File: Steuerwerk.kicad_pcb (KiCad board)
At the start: 2 copper layers, 100 x 160 mm, 115 parts, among them J1 Conn_01x04, J2 Conn_01x02, J3 Conn_01x03, J4 Conn_01x03, J5 Conn_01x02, J6 Conn_01x04, J7 Conn_01x02, J8 Conn_01x04, Q1 Q_PNP_BCE, U1 74LS161, U2 74LS138, U3 74LS138, U4 74240, U5 74LS374, U6 74LS374, U7 74541, U8 74541

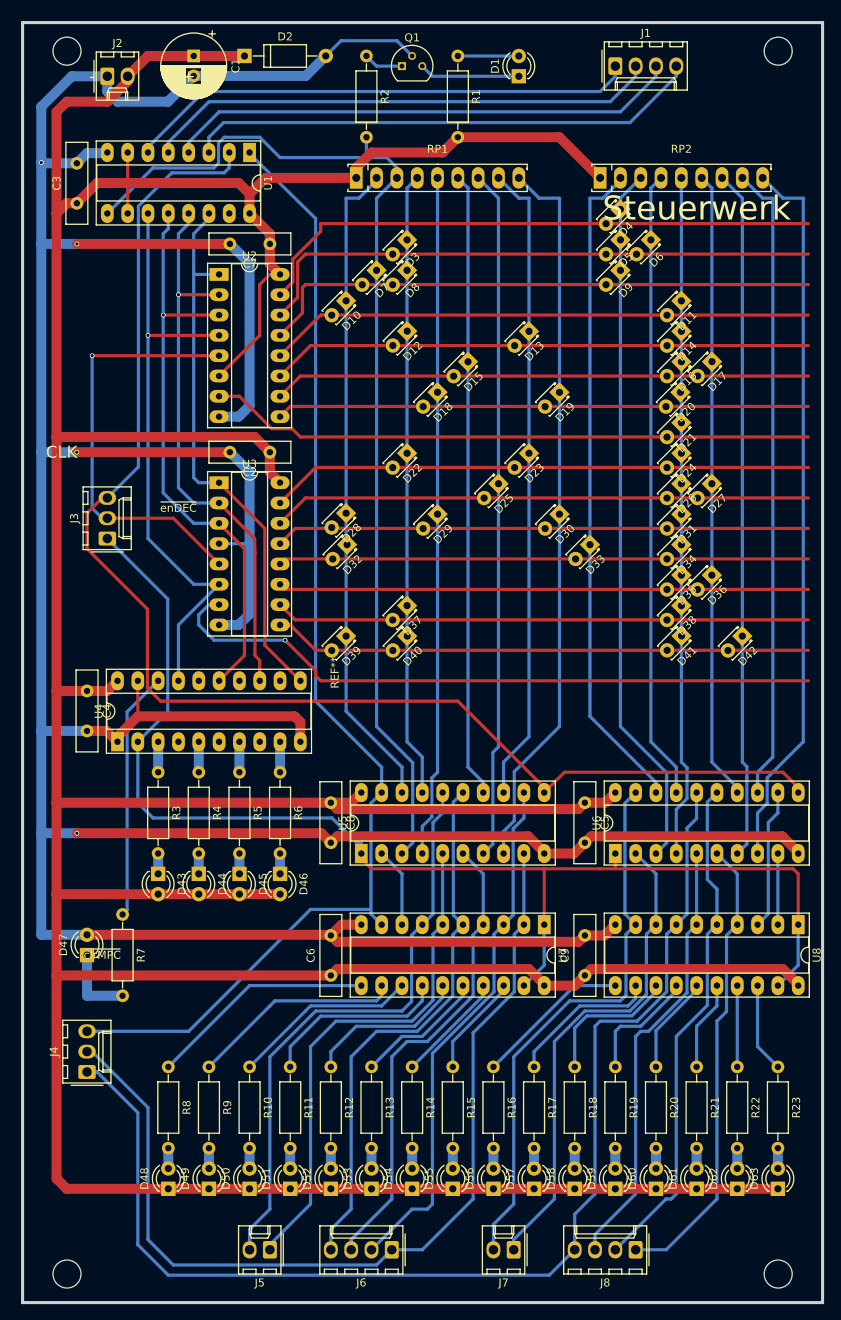
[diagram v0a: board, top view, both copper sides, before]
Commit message: Steuerwerk: - Sperrbereiche für die Köpfe der Befestigungsschrauben hinzugefügt - Beschriftung (Silkscreen) auf der Platinenoberseite bearbeitet
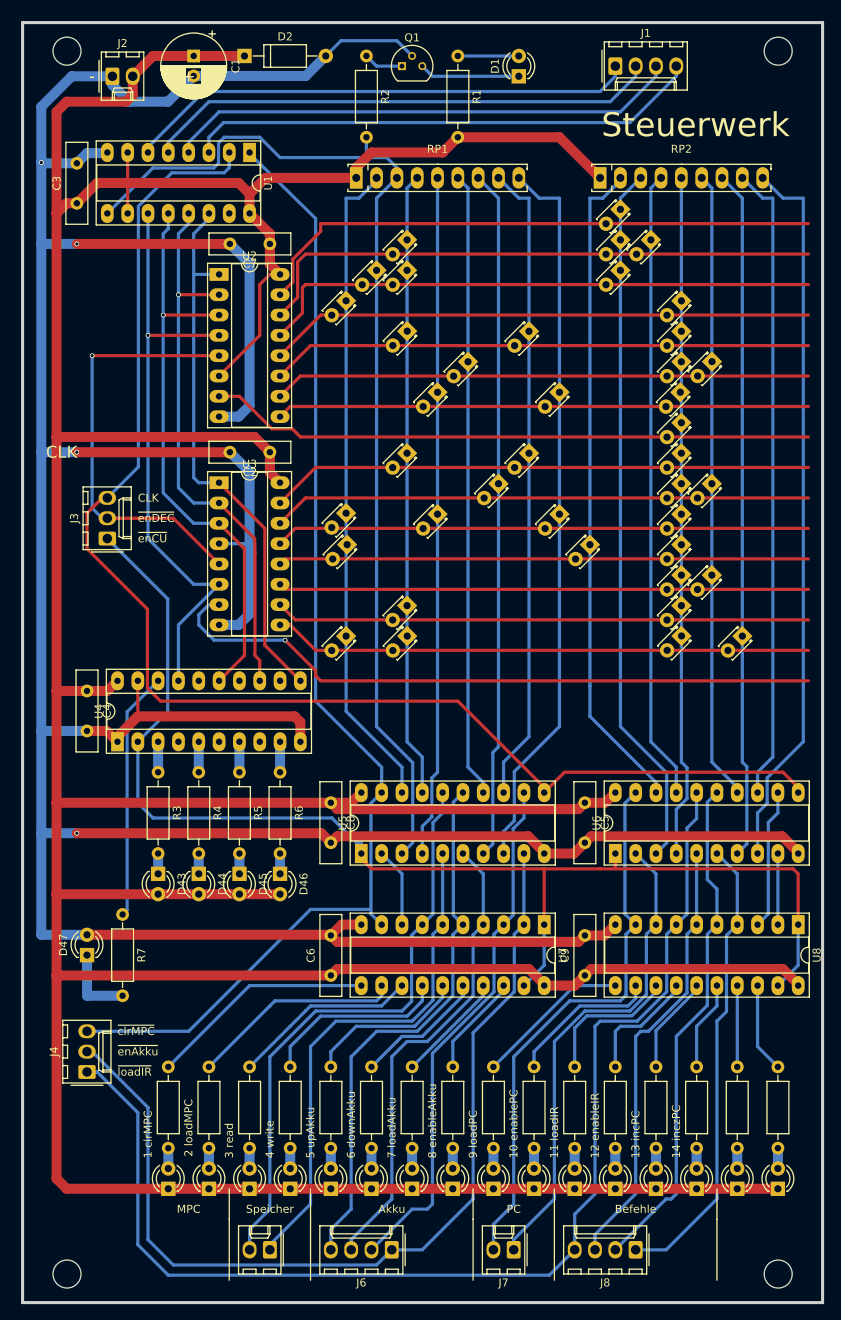
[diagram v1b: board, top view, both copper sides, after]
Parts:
- R1, R10, R11, R12, R13, R14, R15, R16, R17, R18, R19, R2, R20, R21, R22, R23, R3, R4, R5, R6, R7, R8, R9: footprint Resistors_ThroughHole:R_Axial_DIN0207_L6.3mm_D2.5mm_P10.16mm_Horizontal -> Resistor_THT:R_Axial_DIN0207_L6.3mm_D2.5mm_P10.16mm_Horizontal
- REF**: value EuroBoard160mmX100mm_holes -> EuroBoard160mmX100mm_holes_keepout; footprint allBonsaiFootprintsLibs:EuroBoard160mmX100mm_holes -> bonsai:EuroBoard160mmX100mm_holes_keepout
- moved J2 0.64 mm to (52.1, 40.0)
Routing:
- net VCC: track 601.6 -> 602.6 mm
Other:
- board text added: "1 clrMPC"
- board text added: "10 enablePC"
- board text added: "11 loadIR"
- board text added: "12 enableIR"
- board text added: "13 incPC"
- board text added: "14 inczPC"
- board text added: "2 loadMPC"
- board text added: "3 read"
- board text added: "4 write"
- board text added: "5 upAkku"
- board text added: "6 downAkku"
- board text added: "7 loadAkku"
- board text added: "8 enableAkku"
- board text added: "9 loadPC"
- board text added: "Akku"
- board text added: "Befehle"
- board text added: "MPC"
- board text added: "PC"
- board text added: "Speicher"
- board text added: "~enAkku"
- board text added: "~enCU"
- board text added: "~loadIR"

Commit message: viele Kleinigkeiten
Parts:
- D2: footprint Diodes_ThroughHole:D_A-405_P10.16mm_Horizontal -> Diode_THT:D_A-405_P10.16mm_Horizontal
- Q1: footprint TO_SOT_Packages_THT:TO-92_Molded_Narrow -> Package_TO_SOT_THT:TO-92_Inline_Wide
- RP1, RP2: footprint Housings_SIP:SIP9_Housing_BigPads -> Package_SIP:SIP9_Housing_BigPads
- U1, U2, U3: footprint Housings_DIP:DIP-16_W7.62mm_Socket_LongPads -> Package_DIP:DIP-16_W7.62mm_Socket_LongPads
- U5: footprint Housings_DIP:DIP-20_W7.62mm_Socket_LongPads -> Package_DIP:DIP-20_W7.62mm_Socket_LongPads
- U6: footprint tg_foodprint:DIP-20_W7.62mm_Socket_LongPadstg -> Package_DIP:DIP-20_W7.62mm_Socket_LongPads
- moved D47 26.7 mm to (49.6, 176.5), turned to 270 degrees
- moved R7 11.4 mm to (53.4, 133.3)
- moved RP1 10.2 mm to (82.6, 52.7)
- moved RP2 10.2 mm to (113.1, 52.7)
- moved R3 6.35 mm to (57.8, 133.3)
- moved R4 6.35 mm to (62.9, 133.3)
- moved R5 6.35 mm to (68.0, 133.3)
- moved R6 6.35 mm to (73.1, 133.3)
- moved D43 6.35 mm to (57.8, 146.0)
- moved D44 6.35 mm to (62.9, 146.0)
- moved D45 6.35 mm to (68.0, 146.0)
- moved D46 6.35 mm to (73.1, 146.0)
- moved C4 4.44 mm to (48.9, 121.2)
- moved U4 4.44 mm to (52.7, 127.6)
- moved Q1 1.27 mm to (87.0, 38.7)
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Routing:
- net Net-(D47-Pad1): track 9.52 -> 37.2 mm
- net VCC: track 602.6 -> 575.7 mm
- net Net-(R7-Pad1): track 31.1 -> 15.2 mm
- net GND: track 486.2 -> 501.2 mm
- net /Takt: track 171.2 -> 176.0 mm
- net Net-(U1-Pad13): track 70.1 -> 74.5 mm
- net Net-(U1-Pad12): track 73.1 -> 77.5 mm
- net Net-(U1-Pad11): track 75.6 -> 80.0 mm
- net Net-(U1-Pad14): track 69.4 -> 73.8 mm
- net /clrMPC: track 146.1 -> 150.2 mm
- net Net-(J5-Pad2): track 73.5 -> 72.2 mm
- net Net-(R6-Pad1): track 3.81 -> 5.08 mm
- net Net-(R5-Pad1): track 3.81 -> 5.08 mm
- net Net-(R4-Pad1): track 3.81 -> 5.08 mm
- net Net-(R3-Pad1): track 3.81 -> 5.08 mm
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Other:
- board text added: "0"
- board text added: "1"
- board text added: "10"
- board text added: "10 writePC"
- board text added: "11"
- board text added: "11 readIR"
- board text added: "12"
- board text added: "12 writeIR"
- board text added: "13"
- board text added: "14"
- board text added: "14 incPCz"
- board text added: "15"
- board text added: "2"
- board text added: "2 readMPC"
- board text added: "3"
- board text added: "3 writeMem"
- board text added: "4"
- board text added: "4 readMem"
- board text added: "5"
- board text added: "5 incAkku"
- board text added: "6"
- board text added: "6 decAkku"
- board text added: "7"
- board text added: "7 readAkku"
- board text added: "8"
- board text added: "8 writeAkku"
- board text added: "9"
- board text added: "9 readPC"
- board text added: "Mikroprogramm- adresse (MPC)"
- board text added: "enCU"
- board text added: "readMPC"
- board text added: "~readIR"
- board text added: "~writeAkku"
- board text removed: "10 enablePC"
- board text removed: "11 loadIR"
- board text removed: "12 enableIR"
- board text removed: "14 inczPC"
- board text removed: "2 loadMPC"
- board text removed: "3 read"
- board text removed: "4 write"
- board text removed: "5 upAkku"
- board text removed: "6 downAkku"
- board text removed: "7 loadAkku"
- board text removed: "8 enableAkku"
- board text removed: "9 loadPC"
- board text removed: "~enAkku"
- board text removed: "~loadIR"

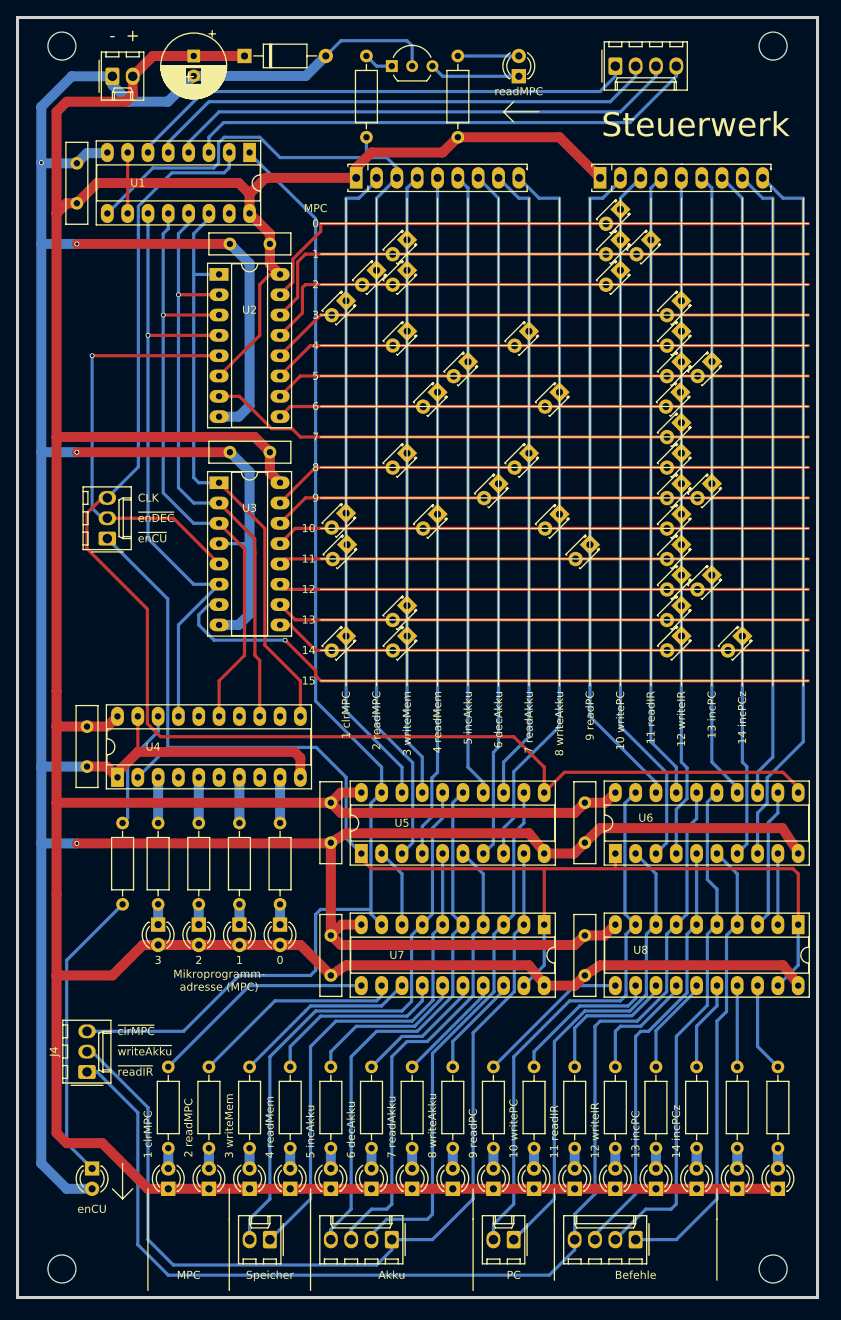
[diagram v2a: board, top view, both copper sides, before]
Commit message: Steuerwerk: Verbinder für die beiden unbenutzten Steuersignale eingebaut
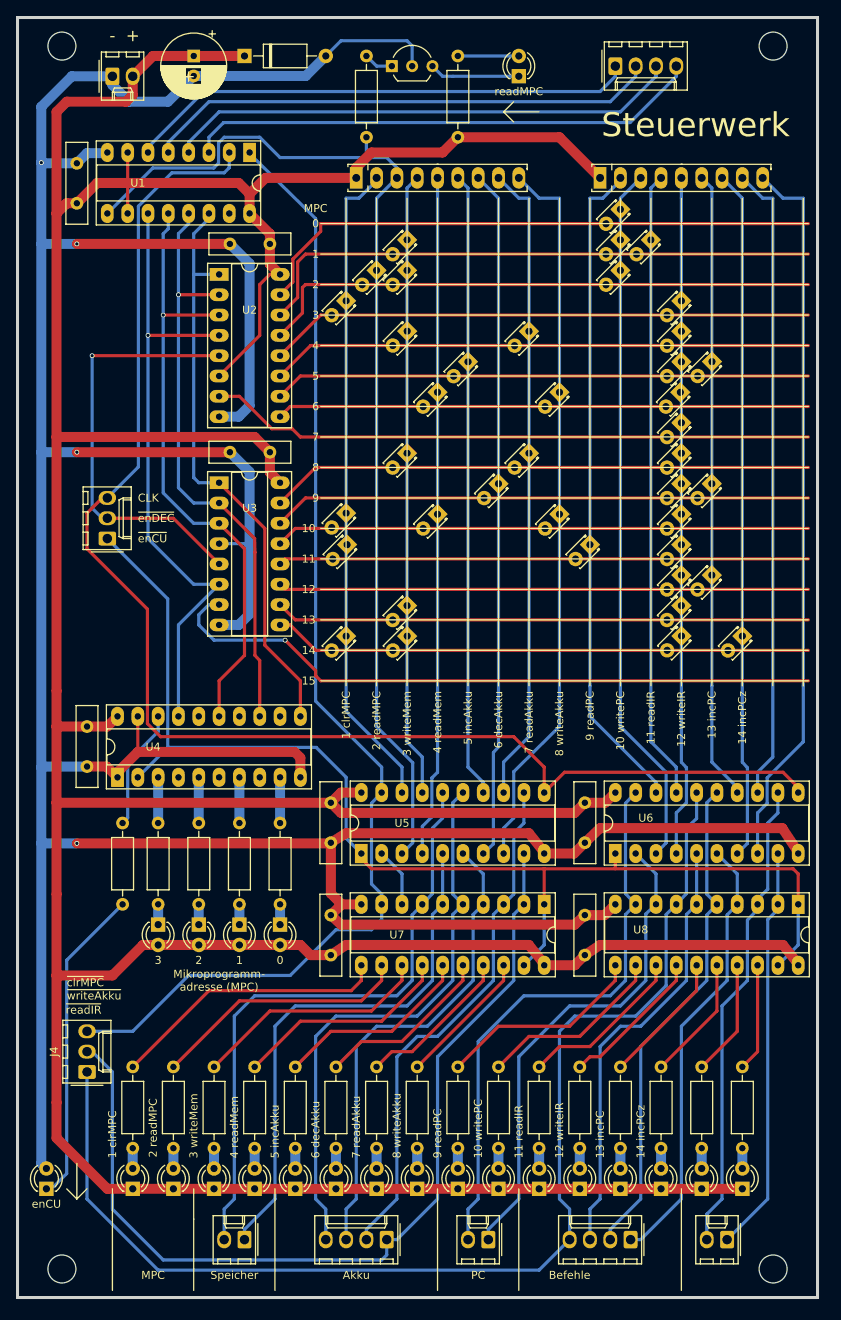
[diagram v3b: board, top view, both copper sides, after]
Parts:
- added J9: Conn_01x02, Connector_Molex:Molex_KK-254_AE-6410-02A_1x02_P2.54mm_Vertical, F.Cu at (128.9, 185.4)
- moved D47 6.25 mm to (43.9, 179.0), turned to 90 degrees
- moved D49 4.45 mm to (59.7, 179.0)
- moved D50 4.45 mm to (64.8, 179.0)
- moved D51 4.45 mm to (69.9, 179.0)
- moved D52 4.45 mm to (75.0, 179.0)
- moved D57 4.45 mm to (100.4, 179.0)
- moved D58 4.45 mm to (105.4, 179.0)
- moved D59 4.45 mm to (110.5, 179.0)
- moved D60 4.45 mm to (115.6, 179.0)
- moved D62 4.45 mm to (125.8, 179.0)
- moved R10 4.45 mm to (64.8, 163.8)
- moved R11 4.45 mm to (69.9, 163.8)
- moved R12 4.45 mm to (75.0, 163.8)
- moved R17 4.45 mm to (100.4, 163.8)
- moved R18 4.45 mm to (105.4, 163.8)
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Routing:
- net Net-(J9-Pad1): track 8.89 -> 50.9 mm
- net Net-(J9-Pad2): track 17.6 -> 59.5 mm
- net GND: track 501.2 -> 491.1 mm
- net Net-(R10-Pad1): track 23.3 -> 29.9 mm
- net Net-(R16-Pad1): track 19.4 -> 26.1 mm
- net Net-(R8-Pad1): track 28.3 -> 35.0 mm
- net Net-(R13-Pad1): track 16.4 -> 22.3 mm
- net Net-(R14-Pad1): track 13.8 -> 19.7 mm
- net Net-(R9-Pad1): track 26.7 -> 32.6 mm
- net Net-(J5-Pad2): track 72.2 -> 77.6 mm
- net VCC: track 575.7 -> 570.5 mm
- net /enSTW: track 157.3 -> 152.2 mm
- net Net-(R15-Pad1): track 12.8 -> 17.8 mm
- net Net-(R20-Pad1): track 12.3 -> 17.2 mm
- net Net-(R12-Pad1): track 20.2 -> 24.8 mm
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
